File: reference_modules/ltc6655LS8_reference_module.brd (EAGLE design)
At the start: 25.4 x 27.3 mm, 8 parts

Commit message: * finished ltc6655 reference board
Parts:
- removed C2: 10u, SquantorRCL:C0805
- added R1: (no value), SquantorRCL:R1206
- added R2: ferrite, SquantorRCL:R0805
- C3: value 2.2u -> 10u; device SquantorRCL:C2824W -> SquantorRCL:C0805
- moved C3 14.7 mm to (4.45, 21.0), turned to 90 degrees
- moved C5 6.63 mm to (12.7, 8.26)
- moved C4 6.63 mm to (6.35, 8.26)
- moved C1 5.43 mm to (8.89, 22.9)
- moved U$1 3.70 mm to (11.4, 18.4)
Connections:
- new net N$1: JP1.1, R2.1
- net GND: now also C3.1; no longer C2.2, C3.2
- net VCC_VREF: now also C3.2, R2.2; no longer C2.1, JP1.1
- net VREF_IN: now also R1.2
- net VREF_OUT: now also R1.1; no longer C3.1
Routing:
- net VREF_OUT: track 6.77 -> 17.0 mm
- net VCC_VREF: track 20.0 -> 14.2 mm
- net VREF_IN: track 15.7 -> 12.9 mm
- net N$1: track 0.00 -> 2.23 mm
- net GND: track 9.89 -> 9.67 mm, vias 5 -> 12
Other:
- board size 25.4 x 27.3 mm -> 25.4 x 26.7 mm

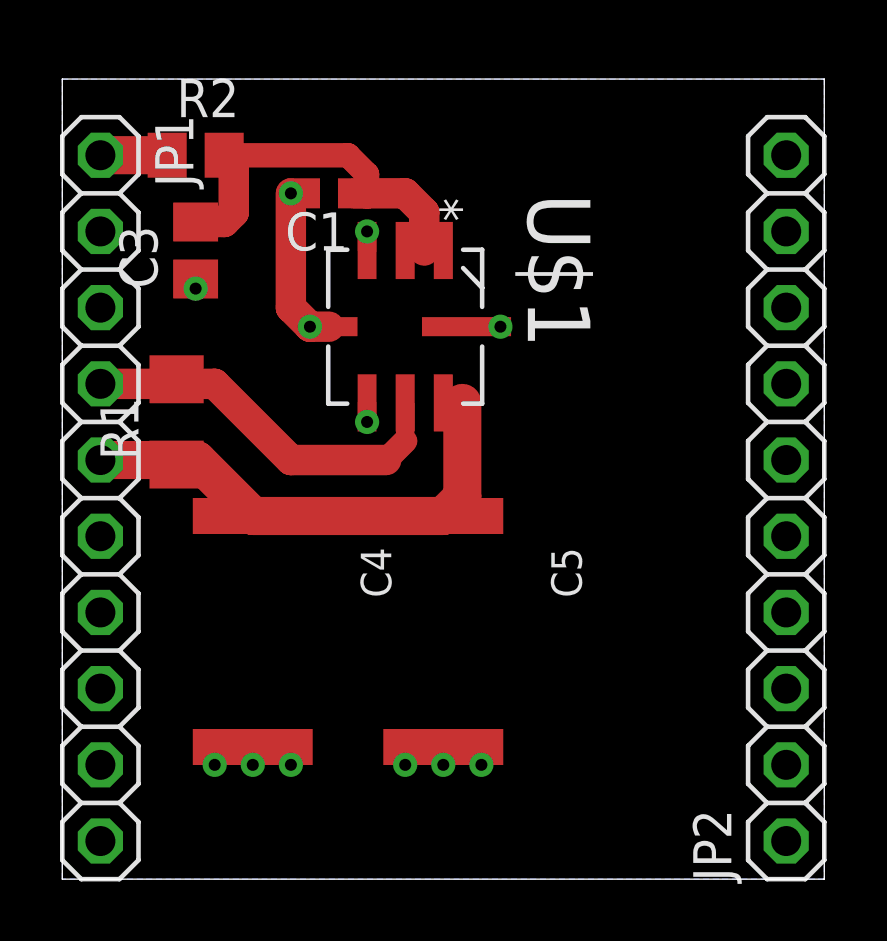
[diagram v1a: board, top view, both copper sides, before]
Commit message: * removed old unused project * switched to module outline layout, this way i am sure the boards will remain the same
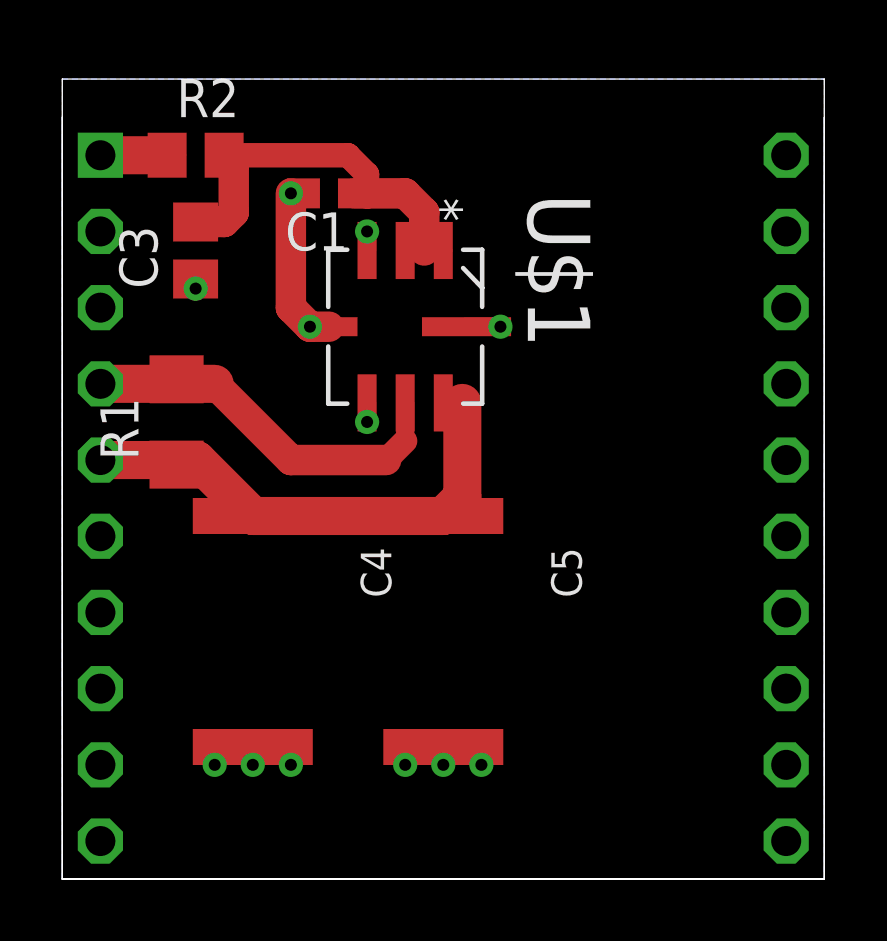
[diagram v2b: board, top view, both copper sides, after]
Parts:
- removed JP1, JP2: (no value), SquantorConnectors:1X10_NORMAL_OCT
- added U$2: METROLOGY_MODULE, SquantorPCBOutline:METROLOGY_MODULE
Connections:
- removed net GND_ADC: JP2.9
- removed net N$13: JP2.3
- removed net N$14: JP2.4
- removed net N$15: JP2.5
- removed net N$16: JP2.6
- removed net N$17: JP2.7
- removed net N$18: JP2.8
- removed net V+: JP1.7
- removed net V-: JP1.10
- removed net VCC_ADC: JP2.10
- removed net VIN+: JP1.8
- removed net VIN-: JP1.9
- net GND: now also U$2.P$2, U$2.P$3, U$2.P$6; no longer JP1.2, JP1.3, JP1.6, JP2.1, JP2.2
- net N$1: now also U$2.P$1; no longer JP1.1
- net VREF_IN: now also U$2.P$4; no longer JP1.4
- net VREF_OUT: now also U$2.P$5; no longer JP1.5
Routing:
- net VREF_IN: track 12.9 -> 14.2 mm
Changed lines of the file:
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@@
 </autorouter>
 <elements>
-<element name="JP1" library="SquantorConnectors" package="1X10_NORMAL_OCT" value="" x="1.27" y="12.7" rot="R270"/>
-<element name="JP2" library="SquantorConnectors" package="1X10_NORMAL_OCT" value="" x="24.13" y="12.7" rot="R90"/>
 <element name="U$1" library="SquantorLinearTechnology" package="LS8_ELONG" value="LTC6655LS8_ELONG" x="11.43" y="18.415" rot="R270"/>
 <element name="C1" library="SquantorRCL" package="C0603" value="100n" x="8.89" y="22.86" rot="R180"/>
@@
 <element name="R2" library="SquantorRCL" package="R0805" value="ferrite" x="4.445" y="24.13"/>
 <element name="C3" library="SquantorRCL" package="C0805" value="10u" x="4.445" y="20.955" rot="R90"/>
+<element name="U$2" library="SquantorPCBOutline" package="METROLOGY_MODULE" value="METROLOGY_MODULE" x="12.7" y="12.7"/>
 </elements>
 <signals>
@@
 </signal>
 <signal name="VREF_IN">
-<contactref element="JP1" pad="4"/>
 <contactref element="U$1" pad="6"/>
 <contactref element="R1" pad="2"/>
@@
 <wire x1="7.62" y1="13.97" x2="5.08" y2="16.51" width="1.016" layer="1"/>
 <wire x1="5.08" y1="16.51" x2="3.81" y2="16.51" width="1.016" layer="1"/>
-<wire x1="3.81" y1="16.51" x2="1.27" y2="16.51" width="1.016" layer="1"/>
 <wire x1="3.81" y1="16.662" x2="3.81" y2="16.51" width="1.016" layer="1"/>
+<contactref element="U$2" pad="P$4"/>
+<wire x1="1.27" y1="16.51" x2="5.08" y2="16.51" width="1.27" layer="1"/>
 </signal>
 <signal name="VREF_OUT">
-<contactref element="JP1" pad="5"/>
 <contactref element="U$1" pad="7"/>
 <contactref element="C5" pad="1"/>
@@
 <wire x1="12.7" y1="12.105" x2="6.35" y2="12.105" width="1.27" layer="1"/>
 <wire x1="6.35" y1="12.105" x2="4.485" y2="13.97" width="1.27" layer="1"/>
-<wire x1="4.485" y1="13.97" x2="3.81" y2="13.97" width="1.27" layer="1"/>
-<wire x1="3.81" y1="13.97" x2="1.27" y2="13.97" width="1.27" layer="1"/>
+<wire x1="4.485" y1="13.97" x2="4.445" y2="13.97" width="1.27" layer="1"/>
+<wire x1="4.445" y1="13.97" x2="3.81" y2="13.97" width="1.27" layer="1"/>
 <wire x1="3.81" y1="13.818" x2="3.81" y2="13.97" width="0.8128" layer="1"/>
-</signal>
-<signal name="V+">
-<contactref element="JP1" pad="7"/>
-</signal>
-<signal name="VIN+">
-<contactref element="JP1" pad="8"/>
-</signal>
-<signal name="VIN-">
-<contactref element="JP1" pad="9"/>
-</signal>
-<signal name="V-">
-<contactref element="JP1" pad="10"/>
+<contactref element="U$2" pad="P$5"/>
+<wire x1="1.27" y1="13.97" x2="3.81" y2="13.97" width="1.27" layer="1"/>
 </signal>
 <signal name="GND">
-<contactref element="JP2" pad="1"/>
-<contactref element="JP2" pad="2"/>
-<contactref element="JP1" pad="2"/>
-<contactref element="JP1" pad="3"/>
-<contactref element="JP1" pad="6"/>
 <contactref element="U$1" pad="4"/>
 <contactref element="U$1" pad="5"/>
@@
 <wire x1="12.7" y1="4.405" x2="12.7" y2="3.81" width="0.6096" layer="1"/>
 <via x="8.255" y="18.415" extent="1-16" drill="0.4" shape="octagon"/>
-</signal>
-<signal name="N$13">
-<contactref element="JP2" pad="3"/>
-</signal>
-<signal name="N$14">
-<contactref element="JP2" pad="4"/>
-</signal>
-<signal name="N$15">
-<contactref element="JP2" pad="5"/>
-</signal>
-<signal name="N$16">
-<contactref element="JP2" pad="6"/>
-</signal>
-<signal name="N$17">
-<contactref element="JP2" pad="7"/>
-</signal>
-<signal name="N$18">
-<contactref element="JP2" pad="8"/>
-</signal>
-<signal name="GND_ADC">
-<contactref element="JP2" pad="9"/>
-</signal>
-<signal name="VCC_ADC">
-<contactref element="JP2" pad="10"/>
+<contactref element="U$2" pad="P$2"/>
+<contactref element="U$2" pad="P$3"/>
+<contactref element="U$2" pad="P$6"/>
 </signal>
 <signal name="N$1">
-<contactref element="JP1" pad="1"/>
+<contactref element="U$2" pad="P$1"/>
 <contactref element="R2" pad="1"/>
 <wire x1="1.27" y1="24.13" x2="3.495" y2="24.13" width="1.27" layer="1"/>

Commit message: * updated board format * made the LTC6655 reference module more compact, hopefully better * small modifications to the MCP355X ADC module
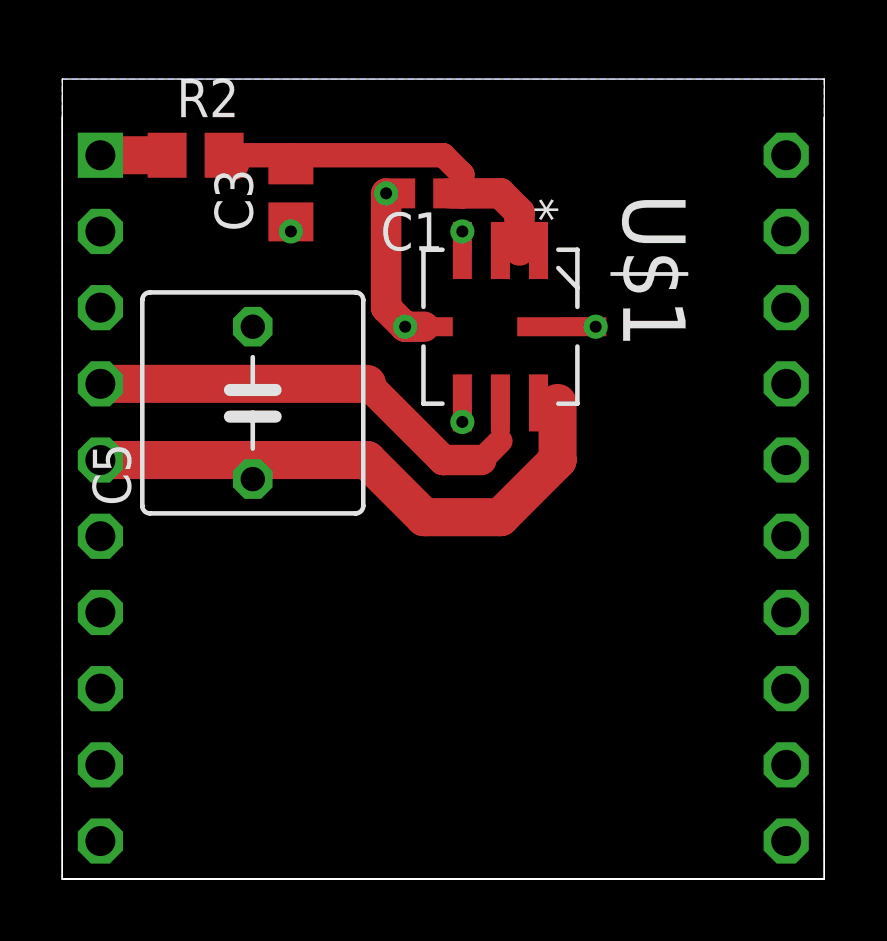
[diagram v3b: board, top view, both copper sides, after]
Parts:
- removed C4: 2.2u, SquantorRCL:C2824W
- removed R1: (no value), SquantorRCL:R1206
- C5: value 2.2u -> 6.8u; device SquantorRCL:C2824W -> SquantorRCL:C050-075X075
- moved C5 9.92 mm to (6.35, 15.9), turned to 90 degrees
- moved C3 3.70 mm to (7.62, 22.9)
- moved U$1 3.18 mm to (14.6, 18.4)
- moved C1 3.17 mm to (12.1, 22.9)
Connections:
- net GND: no longer C4.2
- net VREF_IN: no longer R1.2
- net VREF_OUT: no longer C4.1, R1.1
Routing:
- net VREF_IN: track 14.2 -> 22.3 mm
- net VREF_OUT: track 17.0 -> 20.0 mm
- net GND: track 9.67 -> 8.16 mm, vias 12 -> 6
- net VCC_VREF: track 14.2 -> 14.7 mm
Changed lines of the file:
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@@
 </autorouter>
 <elements>
-<element name="U$1" library="SquantorLinearTechnology" package="LS8_ELONG" value="LTC6655LS8_ELONG" x="11.43" y="18.415" rot="R270"/>
-<element name="C1" library="SquantorRCL" package="C0603" value="100n" x="8.89" y="22.86" rot="R180"/>
-<element name="C4" library="SquantorRCL" package="C2824W" value="2.2u" x="6.35" y="8.255" rot="R270"/>
-<element name="C5" library="SquantorRCL" package="C2824W" value="2.2u" x="12.7" y="8.255" rot="R270"/>
-<element name="R1" library="SquantorRCL" package="R1206" value="" x="3.81" y="15.24" rot="R90"/>
+<element name="U$1" library="SquantorLinearTechnology" package="LS8_ELONG" value="LTC6655LS8_ELONG" x="14.605" y="18.415" rot="R270"/>
+<element name="C1" library="SquantorRCL" package="C0603" value="100n" x="12.065" y="22.86" rot="R180"/>
+<element name="C5" library="SquantorRCL" package="C050-075X075" value="6.8u" x="6.35" y="15.875" rot="R90"/>
 <element name="R2" library="SquantorRCL" package="R0805" value="ferrite" x="4.445" y="24.13"/>
-<element name="C3" library="SquantorRCL" package="C0805" value="10u" x="4.445" y="20.955" rot="R90"/>
+<element name="C3" library="SquantorRCL" package="C0805" value="10u" x="7.62" y="22.86" rot="R90"/>
 <element name="U$2" library="SquantorPCBOutline" package="METROLOGY_MODULE" value="METROLOGY_MODULE" x="12.7" y="12.7"/>
 </elements>
@@
 <contactref element="U$1" pad="2"/>
 <contactref element="U$1" pad="1"/>
-<wire x1="9.74" y1="22.86" x2="10.16" y2="22.86" width="1.016" layer="1"/>
-<wire x1="10.16" y1="22.86" x2="11.43" y2="22.86" width="1.016" layer="1"/>
-<wire x1="11.43" y1="22.86" x2="12.065" y2="22.225" width="1.016" layer="1"/>
-<wire x1="12.065" y1="22.225" x2="12.065" y2="20.955" width="1.016" layer="1"/>
-<wire x1="12.7" y1="20.955" x2="12.065" y2="20.955" width="0.6096" layer="1"/>
+<wire x1="12.915" y1="22.86" x2="13.335" y2="22.86" width="1.016" layer="1"/>
+<wire x1="13.335" y1="22.86" x2="14.605" y2="22.86" width="1.016" layer="1"/>
+<wire x1="14.605" y1="22.86" x2="15.24" y2="22.225" width="1.016" layer="1"/>
+<wire x1="15.24" y1="22.225" x2="15.24" y2="20.955" width="1.016" layer="1"/>
+<wire x1="15.875" y1="20.955" x2="15.24" y2="20.955" width="0.6096" layer="1"/>
 <contactref element="R2" pad="2"/>
 <contactref element="C3" pad="2"/>
-<wire x1="4.445" y1="21.905" x2="5.395" y2="21.905" width="1.016" layer="1"/>
-<wire x1="5.395" y1="21.905" x2="5.715" y2="22.225" width="1.016" layer="1"/>
-<wire x1="5.715" y1="22.225" x2="5.715" y2="23.81" width="1.016" layer="1"/>
 <wire x1="5.715" y1="23.81" x2="5.395" y2="24.13" width="1.016" layer="1"/>
-<wire x1="10.16" y1="22.86" x2="10.16" y2="23.495" width="0.8128" layer="1"/>
-<wire x1="10.16" y1="23.495" x2="9.525" y2="24.13" width="0.8128" layer="1"/>
-<wire x1="9.525" y1="24.13" x2="5.395" y2="24.13" width="0.8128" layer="1"/>
-<wire x1="11.43" y1="20.955" x2="12.065" y2="20.955" width="0.6096" layer="1"/>
+<wire x1="13.335" y1="22.86" x2="13.335" y2="23.495" width="0.8128" layer="1"/>
+<wire x1="13.335" y1="23.495" x2="12.7" y2="24.13" width="0.8128" layer="1"/>
+<wire x1="12.7" y1="24.13" x2="7.62" y2="24.13" width="0.8128" layer="1"/>
+<wire x1="7.62" y1="24.13" x2="5.395" y2="24.13" width="0.8128" layer="1"/>
+<wire x1="14.605" y1="20.955" x2="15.24" y2="20.955" width="0.6096" layer="1"/>
+<wire x1="7.62" y1="23.81" x2="7.62" y2="24.13" width="0.6096" layer="1"/>
 </signal>
 <signal name="VREF_IN">
 <contactref element="U$1" pad="6"/>
-<contactref element="R1" pad="2"/>
-<wire x1="11.43" y1="15.875" x2="11.43" y2="14.605" width="0.6096" layer="1"/>
-<wire x1="11.43" y1="14.605" x2="10.795" y2="13.97" width="0.8128" layer="1"/>
-<wire x1="10.795" y1="13.97" x2="7.62" y2="13.97" width="1.016" layer="1"/>
-<wire x1="7.62" y1="13.97" x2="5.08" y2="16.51" width="1.016" layer="1"/>
-<wire x1="5.08" y1="16.51" x2="3.81" y2="16.51" width="1.016" layer="1"/>
-<wire x1="3.81" y1="16.662" x2="3.81" y2="16.51" width="1.016" layer="1"/>
+<wire x1="14.605" y1="15.875" x2="14.605" y2="14.605" width="0.6096" layer="1"/>
+<wire x1="14.605" y1="14.605" x2="13.97" y2="13.97" width="0.8128" layer="1"/>
+<wire x1="13.97" y1="13.97" x2="12.7" y2="13.97" width="1.016" layer="1"/>
+<wire x1="12.7" y1="13.97" x2="10.16" y2="16.51" width="1.016" layer="1"/>
+<wire x1="10.16" y1="16.51" x2="3.81" y2="16.51" width="1.016" layer="1"/>
 <contactref element="U$2" pad="P$4"/>
-<wire x1="1.27" y1="16.51" x2="5.08" y2="16.51" width="1.27" layer="1"/>
+<wire x1="1.27" y1="16.51" x2="10.16" y2="16.51" width="1.27" layer="1"/>
 </signal>
 <signal name="VREF_OUT">
 <contactref element="U$1" pad="7"/>
 <contactref element="C5" pad="1"/>
-<contactref element="C4" pad="1"/>
-<contactref element="R1" pad="1"/>
-<wire x1="12.7" y1="15.875" x2="13.335" y2="15.875" width="0.6096" layer="1"/>
-<wire x1="13.335" y1="15.875" x2="13.335" y2="12.74" width="1.27" layer="1"/>
-<wire x1="13.335" y1="12.74" x2="12.7" y2="12.105" width="1.27" layer="1"/>
-<wire x1="12.7" y1="12.105" x2="6.35" y2="12.105" width="1.27" layer="1"/>
-<wire x1="6.35" y1="12.105" x2="4.485" y2="13.97" width="1.27" layer="1"/>
-<wire x1="4.485" y1="13.97" x2="4.445" y2="13.97" width="1.27" layer="1"/>
-<wire x1="4.445" y1="13.97" x2="3.81" y2="13.97" width="1.27" layer="1"/>
-<wire x1="3.81" y1="13.818" x2="3.81" y2="13.97" width="0.8128" layer="1"/>
+<wire x1="15.875" y1="15.875" x2="16.51" y2="15.875" width="0.6096" layer="1"/>
 <contactref element="U$2" pad="P$5"/>
-<wire x1="1.27" y1="13.97" x2="3.81" y2="13.97" width="1.27" layer="1"/>
+<wire x1="1.27" y1="13.97" x2="6.35" y2="13.97" width="1.27" layer="1"/>
+<wire x1="6.35" y1="13.97" x2="10.16" y2="13.97" width="1.27" layer="1"/>
+<wire x1="12.065" y1="12.065" x2="10.16" y2="13.97" width="1.27" layer="1"/>
+<wire x1="12.065" y1="12.065" x2="14.605" y2="12.065" width="1.27" layer="1"/>
+<wire x1="14.605" y1="12.065" x2="16.51" y2="13.97" width="1.27" layer="1"/>
+<wire x1="16.51" y1="13.97" x2="16.51" y2="15.875" width="1.27" layer="1"/>
+<wire x1="6.35" y1="13.335" x2="6.35" y2="13.97" width="1.27" layer="1"/>
 </signal>
 <signal name="GND">
@@
 <contactref element="U$1" pad="8"/>
 <contactref element="C5" pad="2"/>
-<contactref element="C4" pad="2"/>
 <contactref element="C1" pad="2"/>
 <polygon width="0.254" layer="16">
@@
 <vertex x="0" y="0"/>
 </polygon>
-<via x="4.445" y="19.685" extent="1-16" drill="0.4" shape="octagon"/>
-<via x="7.62" y="22.86" extent="1-16" drill="0.4" shape="octagon"/>
-<wire x1="8.89" y1="18.415" x2="8.255" y2="18.415" width="1.016" layer="1"/>
-<wire x1="8.255" y1="18.415" x2="7.62" y2="19.05" width="1.016" layer="1"/>
-<wire x1="7.62" y1="19.05" x2="7.62" y2="22.86" width="1.016" layer="1"/>
-<via x="10.16" y="21.59" extent="1-16" drill="0.4" shape="octagon"/>
-<via x="14.605" y="18.415" extent="1-16" drill="0.4" shape="octagon"/>
-<via x="10.16" y="15.24" extent="1-16" drill="0.4" shape="octagon"/>
-<wire x1="10.16" y1="15.875" x2="10.16" y2="15.24" width="0.6096" layer="1"/>
+<via x="7.62" y="21.59" extent="1-16" drill="0.4" shape="octagon"/>
+<via x="10.795" y="22.86" extent="1-16" drill="0.4" shape="octagon"/>
+<wire x1="12.065" y1="18.415" x2="11.43" y2="18.415" width="1.016" layer="1"/>
+<wire x1="11.43" y1="18.415" x2="10.795" y2="19.05" width="1.016" layer="1"/>
+<wire x1="10.795" y1="19.05" x2="10.795" y2="22.86" width="1.016" layer="1"/>
+<via x="13.335" y="21.59" extent="1-16" drill="0.4" shape="octagon"/>
+<via x="17.78" y="18.415" extent="1-16" drill="0.4" shape="octagon"/>
+<via x="13.335" y="15.24" extent="1-16" drill="0.4" shape="octagon"/>
+<wire x1="13.335" y1="15.875" x2="13.335" y2="15.24" width="0.6096" layer="1"/>
 <contactref element="C3" pad="1"/>
-<wire x1="4.445" y1="20.005" x2="4.445" y2="19.685" width="0.8128" layer="1"/>
-<wire x1="7.62" y1="22.86" x2="8.04" y2="22.86" width="0.8128" layer="1"/>
-<wire x1="10.16" y1="21.59" x2="10.16" y2="20.955" width="0.6096" layer="1"/>
-<wire x1="14.605" y1="18.415" x2="13.4747" y2="18.415" width="0.6096" layer="1"/>
-<via x="6.35" y="3.81" extent="1-16" drill="0.4" shape="octagon"/>
-<via x="12.7" y="3.81" extent="1-16" drill="0.4" shape="octagon"/>
-<via x="5.08" y="3.81" extent="1-16" drill="0.4" shape="octagon"/>
-<via x="7.62" y="3.81" extent="1-16" drill="0.4" shape="octagon"/>
-<via x="11.43" y="3.81" extent="1-16" drill="0.4" shape="octagon"/>
-<via x="13.97" y="3.81" extent="1-16" drill="0.4" shape="octagon"/>
-<wire x1="6.35" y1="4.405" x2="6.35" y2="3.81" width="0.6096" layer="1"/>
-<wire x1="12.7" y1="4.405" x2="12.7" y2="3.81" width="0.6096" layer="1"/>
-<via x="8.255" y="18.415" extent="1-16" drill="0.4" shape="octagon"/>
+<wire x1="10.795" y1="22.86" x2="11.215" y2="22.86" width="0.8128" layer="1"/>
+<wire x1="13.335" y1="21.59" x2="13.335" y2="20.955" width="0.6096" layer="1"/>
+<wire x1="17.78" y1="18.415" x2="16.6497" y2="18.415" width="0.6096" layer="1"/>
+<via x="11.43" y="18.415" extent="1-16" drill="0.4" shape="octagon"/>
 <contactref element="U$2" pad="P$2"/>
 <contactref element="U$2" pad="P$3"/>
 <contactref element="U$2" pad="P$6"/>
+<wire x1="7.62" y1="21.59" x2="7.62" y2="21.91" width="0" layer="19" extent="1-1"/>
 </signal>
 <signal name="N$1">

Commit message: * modified boards and processed for production
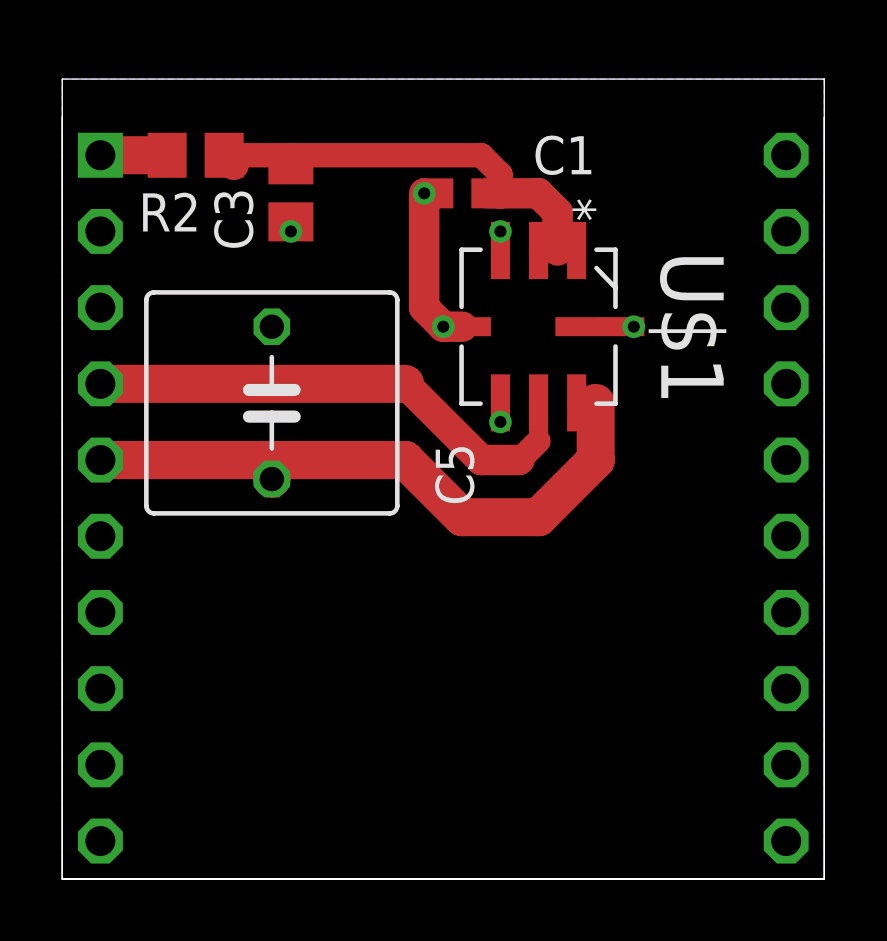
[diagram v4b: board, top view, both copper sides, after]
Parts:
- C5: device SquantorRCL:C050-075X075 -> SquantorRCL:C050-085X075W
- moved C1 1.27 mm to (13.3, 22.9)
- moved U$1 1.27 mm to (15.9, 18.4)
- moved C5 0.64 mm to (6.99, 15.9)
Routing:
- net VREF_IN: track 22.3 -> 24.8 mm
- net VCC_VREF: track 14.7 -> 16.0 mm
- net VREF_OUT: track 20.0 -> 21.3 mm
